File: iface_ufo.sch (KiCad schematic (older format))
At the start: 2 parts, among them J6000 CW308_TARGETCON, J6200 CW_PWR

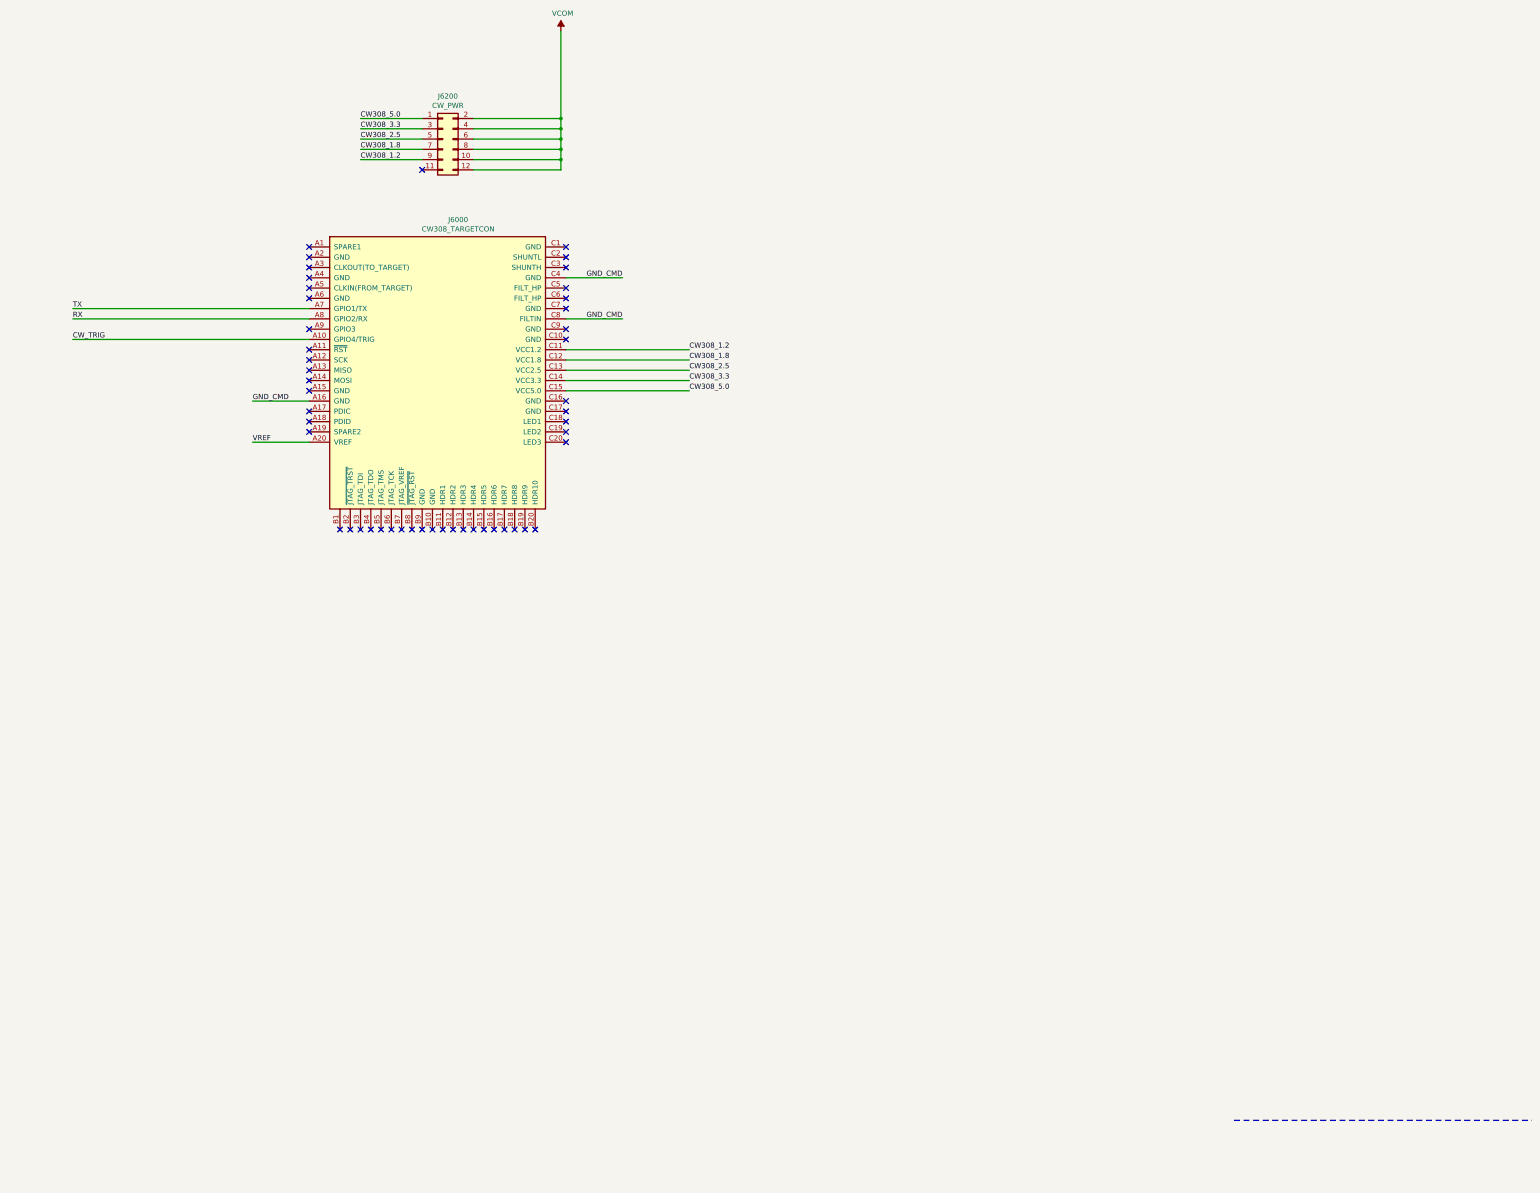
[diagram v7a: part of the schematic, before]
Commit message: [update] switch to Cw 20 pin connector
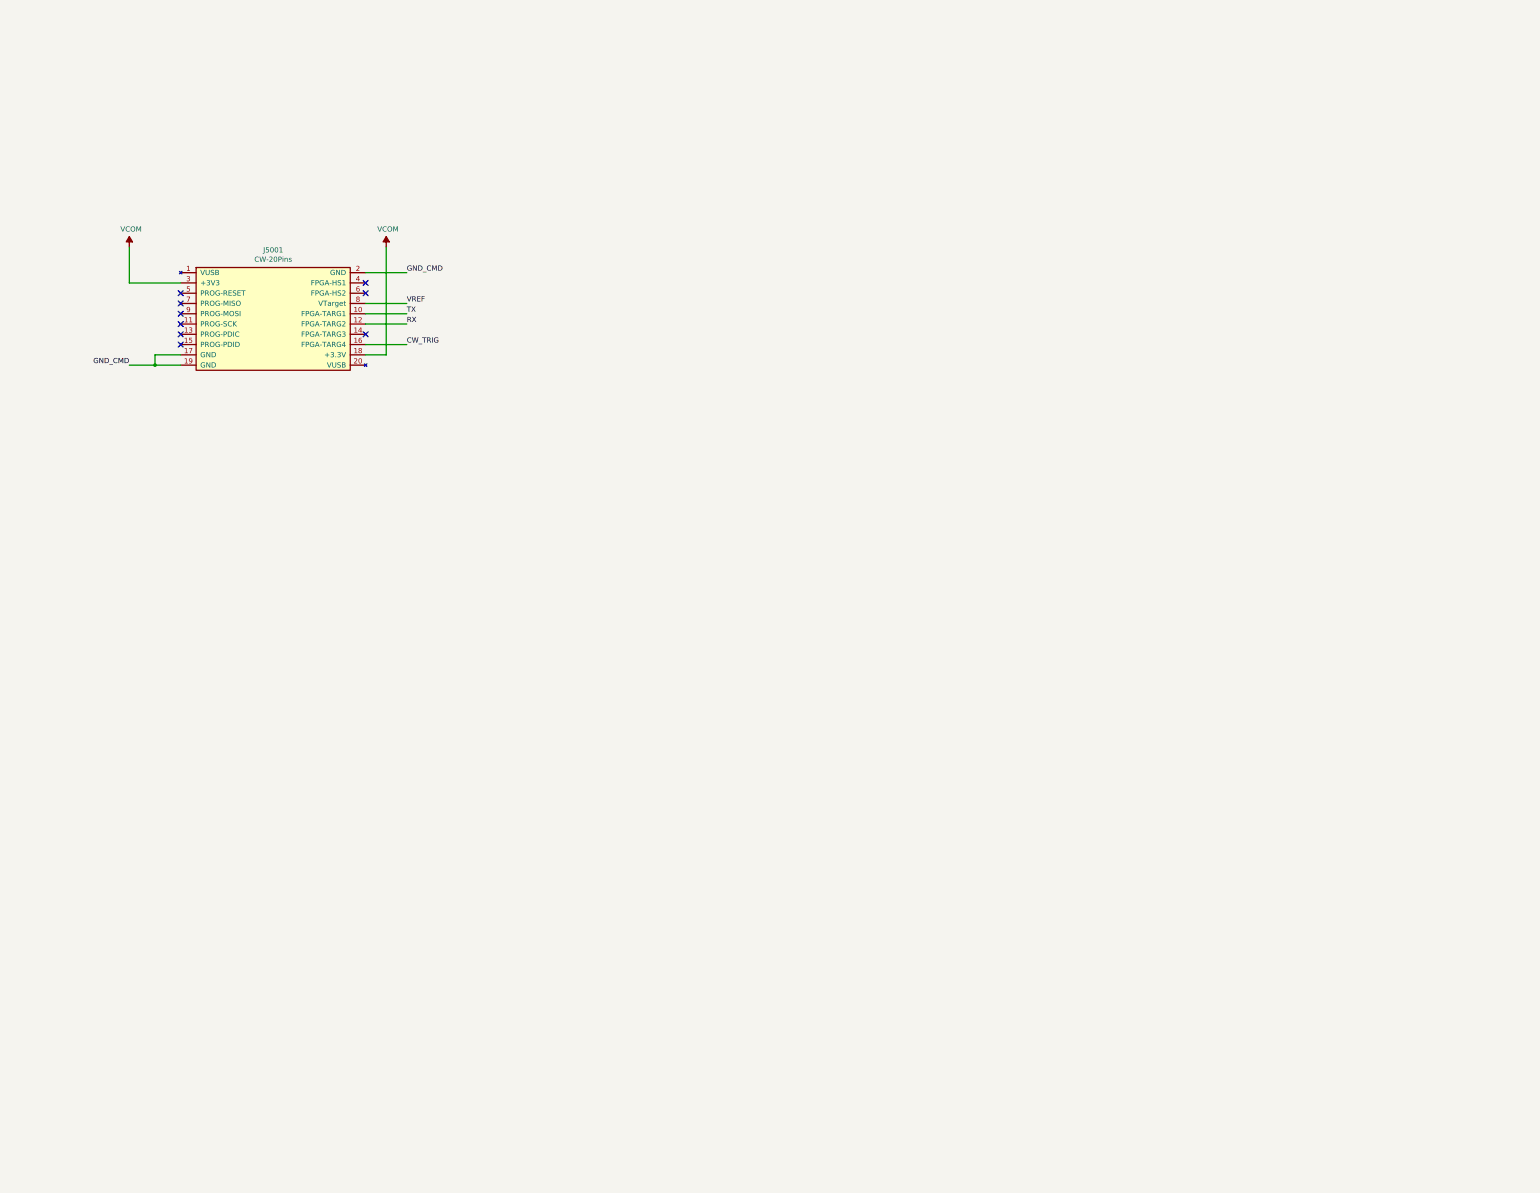
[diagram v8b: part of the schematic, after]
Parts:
- removed J6000: CW308_TARGETCON, leia:CW308T_CONNBOARD, symbol wisp:CW308_TARGETCON
- removed J6200: CW_PWR, Connector_PinHeader_2.54mm:PinHeader_2x06_P2.54mm_Vertical, symbol Connector_Generic:Conn_02x06_Odd_Even
- added J5001: CW-20Pins, Connector_PinHeader_2.54mm:PinHeader_2x10_P2.54mm_Vertical, symbol cw-20pins:CW-20Pins
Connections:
- net CW_TRIG: now also J5001.16 (FPGA-TARG4)
- net RX: now also J5001.12 (FPGA-TARG2)
- net TARGET_GND: now also J5001.17 (GND), J5001.19 (GND), J5001.2 (GND)
- net TX: now also J5001.10 (FPGA-TARG1)
- net VCOM: now also J5001.18 (+3.3V), J5001.3 (+3V3)
- net VREF: now also J5001.8 (VTarget)
- no-connect marks 49 -> 9
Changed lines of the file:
@@
 $Descr A2 23386 16535
 encoding utf-8
-Sheet 4 5
+Sheet 5 5
 Title "CW-LEIA"
 Date "2016-28-20"
 Rev "0.2"
-Comp "ANSSI"
+Comp "H2LAB"
 Comment1 "Designed by Mathieu RENARD"
 Comment2 "LICENCE: CERN Open Hardware Licence v1.2"
@@
 Comment9 ""
 $EndDescr
-Connection ~ 13050 4850
-Connection ~ 13050 4950
-Connection ~ 13050 5050
-Connection ~ 13050 5150
-Connection ~ 13050 5250
-NoConn ~ 12300 8850
-NoConn ~ 12400 8850
-NoConn ~ 12500 8850
-NoConn ~ 12600 8850
-NoConn ~ 12700 8850
-NoConn ~ 12800 8850
-NoConn ~ 10600 7700
-NoConn ~ 10600 7100
-NoConn ~ 10600 6900
-NoConn ~ 10600 6500
-NoConn ~ 10600 6100
-NoConn ~ 11000 8850
-NoConn ~ 11100 8850
-NoConn ~ 11200 8850
-NoConn ~ 11700 8850
-NoConn ~ 11800 8850
-NoConn ~ 12000 8850
-NoConn ~ 12200 8850
-NoConn ~ 10600 7500
-NoConn ~ 10600 6400
-NoConn ~ 10600 6200
-NoConn ~ 13100 6500
-NoConn ~ 13100 6600
-NoConn ~ 13100 6700
-NoConn ~ 13100 6900
-NoConn ~ 13100 7000
-NoConn ~ 13100 7600
-NoConn ~ 11700 5350
-NoConn ~ 13100 7800
-NoConn ~ 13100 7900
-NoConn ~ 13100 8000
-NoConn ~ 10600 7900
-NoConn ~ 10600 7800
-NoConn ~ 10600 6600
-NoConn ~ 10600 6300
-NoConn ~ 13100 6100
-NoConn ~ 10600 7200
-NoConn ~ 10600 7300
-NoConn ~ 10600 7400
-NoConn ~ 11300 8850
-NoConn ~ 11400 8850
-NoConn ~ 11500 8850
-NoConn ~ 11600 8850
-NoConn ~ 11900 8850
-NoConn ~ 12100 8850
-NoConn ~ 13100 6200
-NoConn ~ 13100 6300
-NoConn ~ 10900 8850
-NoConn ~ 13100 7700
+Connection ~ 9100 7250
+NoConn ~ 9350 6550
+NoConn ~ 9350 6650
+NoConn ~ 9350 6750
+NoConn ~ 9350 6850
+NoConn ~ 9350 6950
+NoConn ~ 9350 7050
+NoConn ~ 11150 6450
+NoConn ~ 11150 6550
+NoConn ~ 11150 6950
 Wire Wire Line
 	3650 7500 4750 7500
@@
 	4750 7400 3650 7400
 Wire Wire Line
-	10600 6700 8300 6700
+	8850 6450 8850 6100
 Wire Wire Line
-	10600 6800 8300 6800
+	8850 6450 9350 6450
 Wire Wire Line
-	10600 7000 8300 7000
+	8850 7250 9100 7250
 Wire Wire Line
-	10600 7600 10050 7600
+	9100 7150 9100 7250
 Wire Wire Line
-	10600 8000 10050 8000
+	9100 7250 9350 7250
 Wire Wire Line
-	11100 5250 11700 5250
+	9350 7150 9100 7150
 Wire Wire Line
-	11700 4850 11100 4850
+	11150 6350 11550 6350
 Wire Wire Line
-	11700 4950 11100 4950
+	11150 6650 11550 6650
 Wire Wire Line
-	11700 5050 11100 5050
+	11150 6750 11550 6750
 Wire Wire Line
-	11700 5150 11100 5150
+	11150 6850 11550 6850
 Wire Wire Line
-	12200 4850 13050 4850
+	11150 7050 11550 7050
 Wire Wire Line
-	12200 4950 13050 4950
+	11150 7150 11350 7150
 Wire Wire Line
-	12200 5050 13050 5050
-Wire Wire Line
-	12200 5150 13050 5150
-Wire Wire Line
-	12200 5250 13050 5250
-Wire Wire Line
-	12200 5350 13050 5350
-Wire Wire Line
-	13050 4000 13050 4850
-Wire Wire Line
-	13050 4950 13050 4850
-Wire Wire Line
-	13050 5050 13050 4950
-Wire Wire Line
-	13050 5150 13050 5050
-Wire Wire Line
-	13050 5250 13050 5150
-Wire Wire Line
-	13050 5350 13050 5250
-Wire Wire Line
-	13100 6400 13650 6400
-Wire Wire Line
-	13100 6800 13650 6800
-Wire Wire Line
-	13100 7100 14300 7100
-Wire Wire Line
-	13100 7200 14300 7200
-Wire Wire Line
-	13100 7300 14300 7300
-Wire Wire Line
-	13100 7400 14300 7400
-Wire Wire Line
-	13100 7500 14300 7500
-Wire Notes Line
-	19600 14600 22500 14600
+	11350 6100 11350 7150
 Text Label -16800 27400 0    81   ~ 0
 ear
@@
 Text Label 4950 6600 2    50   ~ 0
 GND_CMD
-Text Label 8300 6700 0    50   ~ 0
+Text Label 8850 7250 2    50   ~ 0
+GND_CMD
+Text Label 11550 6350 0    50   ~ 0
+GND_CMD
+Text Label 11550 6650 0    50   ~ 0
+VREF
+Text Label 11550 6750 0    50   ~ 0
 TX
-Text Label 8300 6800 0    50   ~ 0
+Text Label 11550 6850 0    50   ~ 0
 RX
-Text Label 8300 7000 0    50   ~ 0
+Text Label 11550 7050 0    50   ~ 0
 CW_TRIG
-Text Label 10050 7600 0    50   ~ 0
-GND_CMD
-Text Label 10050 8000 0    50   ~ 0
-VREF
-Text Label 11100 4850 0    50   ~ 0
-CW308_5.0
-Text Label 11100 4950 0    50   ~ 0
-CW308_3.3
-Text Label 11100 5050 0    50   ~ 0
-CW308_2.5
-Text Label 11100 5150 0    50   ~ 0
-CW308_1.8
-Text Label 11100 5250 0    50   ~ 0
-CW308_1.2
-Text Label 13650 6400 2    50   ~ 0
-GND_CMD
-Text Label 13650 6800 2    50   ~ 0
-GND_CMD
-Text Label 14300 7100 0    50   ~ 0
-CW308_1.2
-Text Label 14300 7200 0    50   ~ 0
-CW308_1.8
-Text Label 14300 7300 0    50   ~ 0
-CW308_2.5
-Text Label 14300 7400 0    50   ~ 0
-CW308_3.3
-Text Label 14300 7500 0    50   ~ 0
-CW308_5.0
 Text HLabel 3650 7400 0    50   Input ~ 0
 CW_TRIG
@@
 $EndComp
 $Comp
-L power:VCOM #PWR0125
-U 1 1 5C6F92F0
-P 13050 4000
-F 0 "#PWR0125" H 13050 3850 50  0001 C CNN
-F 1 "VCOM" H 13067 4173 50  0000 C CNN
-F 2 "" H 13050 4000 50  0001 C CNN
-F 3 "" H 13050 4000 50  0001 C CNN
-	1    13050 4000
+L power:VCOM #PWR05001
+U 1 1 5EE13333
+P 8850 6100
+F 0 "#PWR05001" H 8850 5950 50  0001 C CNN
+F 1 "VCOM" H 8867 6273 50  0000 C CNN
+F 2 "" H 8850 6100 50  0001 C CNN
+F 3 "" H 8850 6100 50  0001 C CNN
+	1    8850 6100
 	1    0    0    -1
 $EndComp
 $Comp
-L Connector_Generic:Conn_02x06_Odd_Even J6200
-U 1 1 5C47892C
-P 11900 5050
-F 0 "J6200" H 11950 5467 50  0000 C CNN
-F 1 "CW_PWR" H 11950 5376 50  0000 C CNN
-F 2 "Connector_PinHeader_2.54mm:PinHeader_2x06_P2.54mm_Vertical" H 11900 5050 50  0001 C CNN
-F 3 "~" H 11900 5050 50  0001 C CNN
-F 4 "Molex" H 11900 5050 50  0001 C CNN "MFG Name"
-F 5 "90131-0766" H 11900 5050 50  0001 C CNN "MFG Part Num"
-F 6 "WM8142-ND" H 11900 5050 50  0001 C CNN "Distrib PN"
-F 7 "Digi-key" H 11900 5050 50  0001 C CNN "Distrib"
-F 8 "Digi-key" H -5250 -1950 50  0001 C CNN "Distrib Name"
-	1    11900 5050
+L power:VCOM #PWR05002
+U 1 1 5EE16BD9
+P 11350 6100
+F 0 "#PWR05002" H 11350 5950 50  0001 C CNN
+F 1 "VCOM" H 11367 6273 50  0000 C CNN
+F 2 "" H 11350 6100 50  0001 C CNN
+F 3 "" H 11350 6100 50  0001 C CNN
+	1    11350 6100
 	1    0    0    -1
 $EndComp
 $Comp
-L wisp:CW308_TARGETCON J6000
-U 1 1 5C2850A5
-P 11800 7000
-F 0 "J6000" H 12050 8165 50  0000 C CNN
-F 1 "CW308_TARGETCON" H 12050 8074 50  0000 C CNN
-F 2 "leia:CW308T_CONNBOARD" H 11800 7000 50  0001 C CNN
-F 3 "" H 11800 7000 50  0001 C CNN
-	1    11800 7000
+L cw-20pins:CW-20Pins J5001
+U 1 1 5EDF746F
+P 9550 6750
+F 0 "J5001" H 10250 7370 50  0000 C CNN
+F 1 "CW-20Pins" H 10250 7279 50  0000 C CNN
+F 2 "Connector_PinHeader_2.54mm:PinHeader_2x10_P2.54mm_Vertical" H 9550 6750 50  0001 C CNN
+F 3 "http://www.farnell.com/datasheets/2786059.pdf" H 9550 6750 50  0001 C CNN
+F 4 "Farnell" H 9550 6750 50  0001 C CNN "Distrib"
+F 5 "https://fr.farnell.com/molex/70246-2004/connect-header-20-voies-2-rangs/dp/1392410" H 9550 6750 50  0001 C CNN "Distrib Link"
+F 6 "Farnell" H 9550 6750 50  0001 C CNN "Distrib Name"
+F 7 "1392410" H 9550 6750 50  0001 C CNN "Distrib PN"
+F 8 "1392410" H 9550 6750 50  0001 C CNN "Distrib Part Num"
+F 9 "Molex" H 9550 6750 50  0001 C CNN "MFG Name"
+F 10 "70246-2004" H 9550 6750 50  0001 C CNN "MFG Part Num"
+	1    9550 6750
 	1    0    0    -1
 $EndComp
